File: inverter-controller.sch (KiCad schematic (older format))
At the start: 0 parts

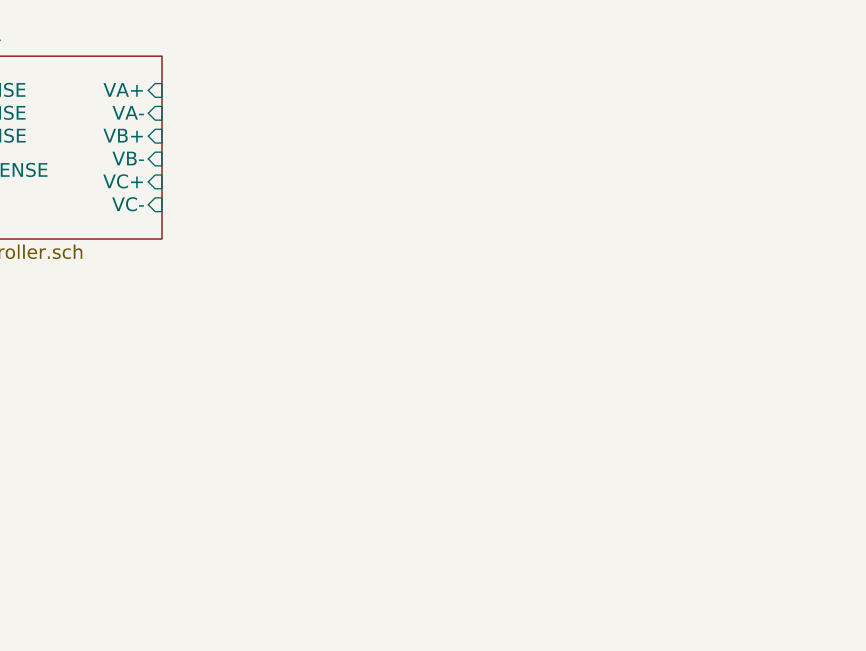
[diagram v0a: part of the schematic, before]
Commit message: Adding IGBT connectors.
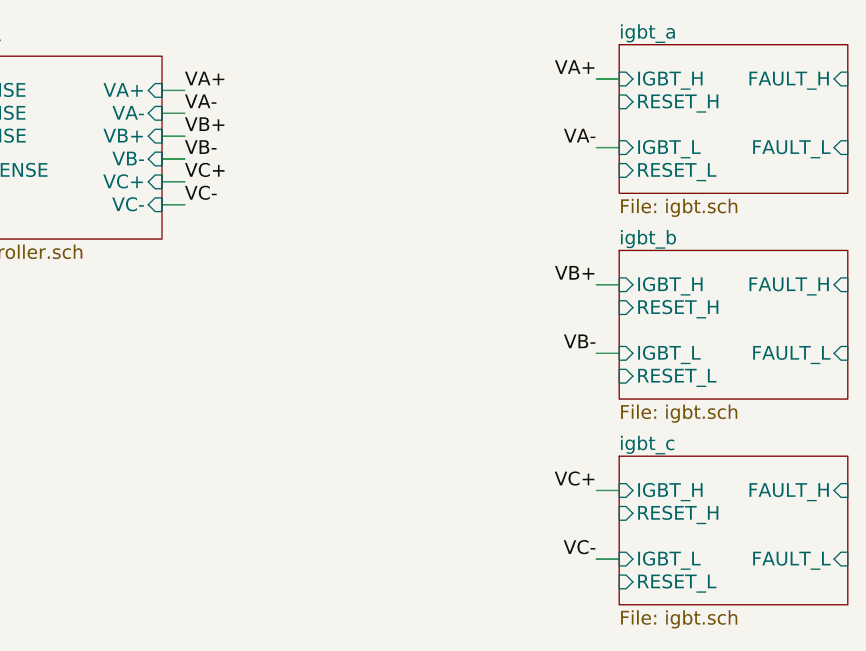
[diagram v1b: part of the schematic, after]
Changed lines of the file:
@@
 LIBS:valves
 LIBS:inverter-controller
+LIBS:inverter-controller-cache
 EELAYER 25 0
 EELAYER END
 $Descr A4 11693 8268
 encoding utf-8
-Sheet 1 3
+Sheet 1 6
 Title ""
 Date ""
@@
 Wire Wire Line
 	1400 1150 2750 1150
+$Sheet
+S 5850 600  1000 650
+U 5AED5DDF
+F0 "igbt_a" 60
+F1 "igbt.sch" 60
+F2 "IGBT_H" I L 5850 750 60
+F3 "IGBT_L" I L 5850 1050 60
+F4 "FAULT_H" I R 6850 750 60
+F5 "RESET_H" I L 5850 850 60
+F6 "FAULT_L" I R 6850 1050 60
+F7 "RESET_L" I L 5850 1150 60
+$EndSheet
+Text Label 3950 800  0    60   ~ 0
+VA+
+Text Label 3950 900  0    60   ~ 0
+VA-
+Text Label 3950 1000 0    60   ~ 0
+VB+
+Text Label 3950 1100 0    60   ~ 0
+VB-
+Text Label 3950 1200 0    60   ~ 0
+VC+
+Text Label 3950 1300 0    60   ~ 0
+VC-
+Text Label 5750 750  2    60   ~ 0
+VA+
+Text Label 5750 1050 2    60   ~ 0
+VA-
+Wire Wire Line
+	5750 750  5850 750
+Wire Wire Line
+	5750 1050 5850 1050
+Wire Wire Line
+	3950 800  3850 800
+Wire Wire Line
+	3850 900  3950 900
+Wire Wire Line
+	3850 1000 3950 1000
+Wire Wire Line
+	3850 1100 3950 1100
+Wire Wire Line
+	3850 1200 3950 1200
+Wire Wire Line
+	3850 1300 3950 1300
+$Sheet
+S 5850 1500 1000 650
+U 5AEDA321
+F0 "igbt_b" 60
+F1 "igbt.sch" 60
+F2 "IGBT_H" I L 5850 1650 60
+F3 "IGBT_L" I L 5850 1950 60
+F4 "FAULT_H" I R 6850 1650 60
+F5 "RESET_H" I L 5850 1750 60
+F6 "FAULT_L" I R 6850 1950 60
+F7 "RESET_L" I L 5850 2050 60
+$EndSheet
+Text Label 5750 1650 2    60   ~ 0
+VB+
+Text Label 5750 1950 2    60   ~ 0
+VB-
+Wire Wire Line
+	5750 1650 5850 1650
+Wire Wire Line
+	5750 1950 5850 1950
+$Sheet
+S 5850 2400 1000 650
+U 5AEDAF6D
+F0 "igbt_c" 60
+F1 "igbt.sch" 60
+F2 "IGBT_H" I L 5850 2550 60
+F3 "IGBT_L" I L 5850 2850 60
+F4 "FAULT_H" I R 6850 2550 60
+F5 "RESET_H" I L 5850 2650 60
+F6 "FAULT_L" I R 6850 2850 60
+F7 "RESET_L" I L 5850 2950 60
+$EndSheet
+Text Label 5750 2550 2    60   ~ 0
+VC+
+Text Label 5750 2850 2    60   ~ 0
+VC-
+Wire Wire Line
+	5750 2550 5850 2550
+Wire Wire Line
+	5750 2850 5850 2850
 $EndSCHEMATC

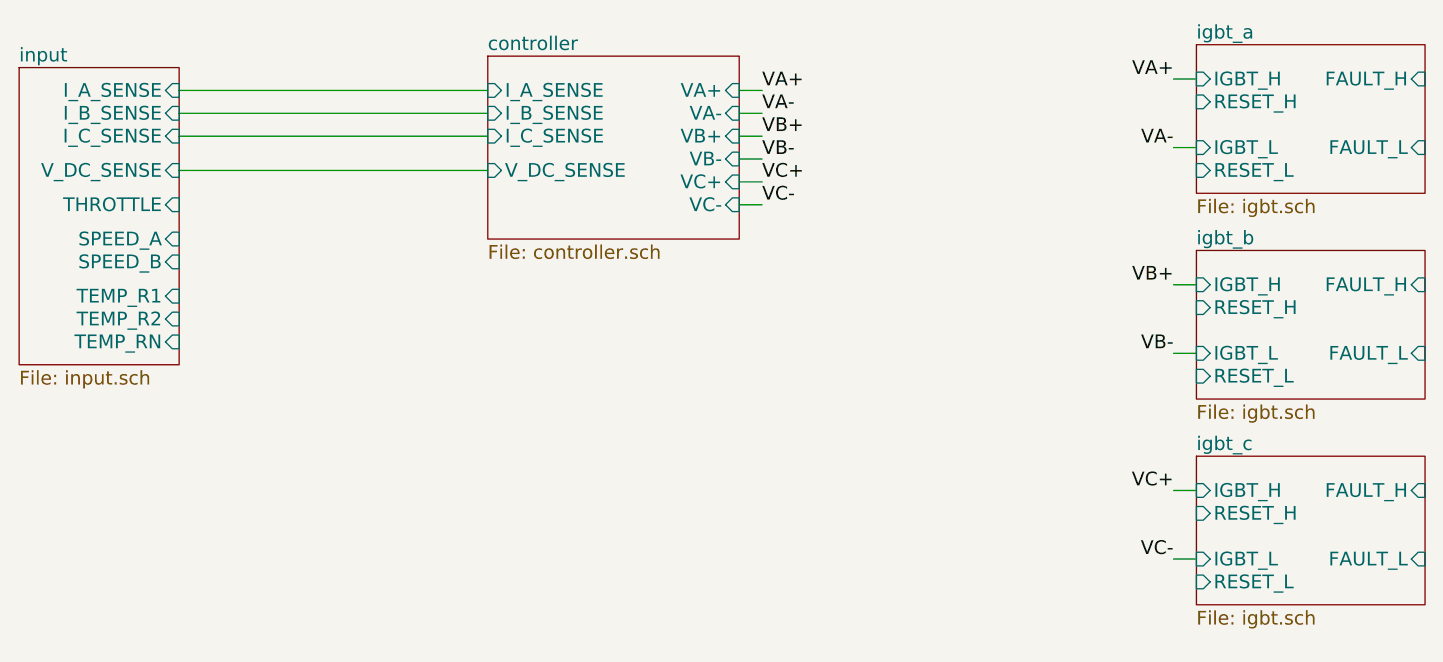
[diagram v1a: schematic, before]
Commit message: Break up input into separate schematics.
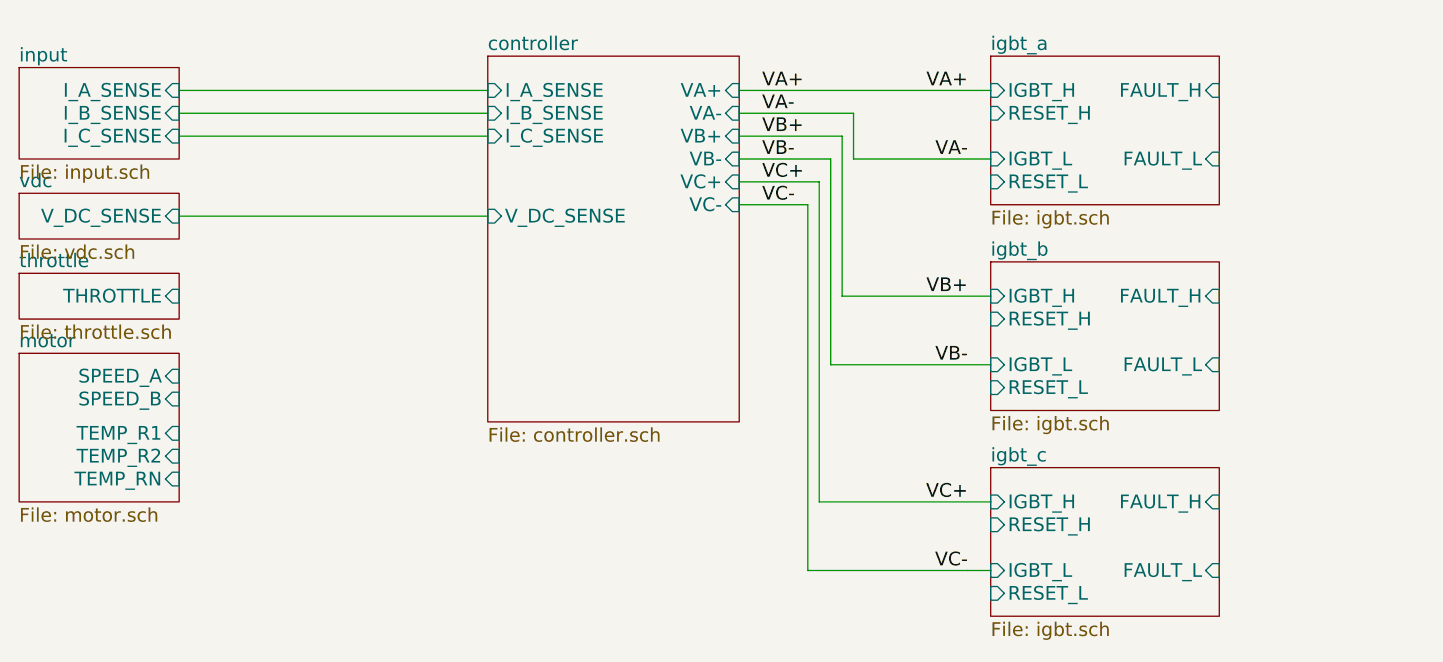
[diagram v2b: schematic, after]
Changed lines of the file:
@@
 $Descr A4 11693 8268
 encoding utf-8
-Sheet 1 6
+Sheet 1 9
 Title ""
 Date ""
@@
 $EndDescr
 $Sheet
-S 2750 650  1100 800
+S 2750 650  1100 1600
 U 5AEC1F05
 F0 "controller" 60
@@
 F9 "I_B_SENSE" I L 2750 900 60
 F10 "I_C_SENSE" I L 2750 1000 60
-F11 "V_DC_SENSE" I L 2750 1150 60
+F11 "V_DC_SENSE" I L 2750 1350 60
 $EndSheet
 $Sheet
-S 700  700  700  1300
-U 5AEC7636
-F0 "input" 60
-F1 "input.sch" 60
-F2 "I_A_SENSE" I R 1400 800 60
-F3 "I_B_SENSE" I R 1400 900 60
-F4 "I_C_SENSE" I R 1400 1000 60
-F5 "V_DC_SENSE" I R 1400 1150 60
-F6 "THROTTLE" I R 1400 1300 60
-F7 "SPEED_A" I R 1400 1450 60
-F8 "SPEED_B" I R 1400 1550 60
-F9 "TEMP_R1" I R 1400 1700 60
-F10 "TEMP_R2" I R 1400 1800 60
-F11 "TEMP_RN" I R 1400 1900 60
-$EndSheet
-Wire Wire Line
-	1400 800  2750 800
-Wire Wire Line
-	1400 900  2750 900
-Wire Wire Line
-	1400 1000 2750 1000
-Wire Wire Line
-	1400 1150 2750 1150
-$Sheet
-S 5850 600  1000 650
+S 4950 650  1000 650
 U 5AED5DDF
 F0 "igbt_a" 60
 F1 "igbt.sch" 60
-F2 "IGBT_H" I L 5850 750 60
-F3 "IGBT_L" I L 5850 1050 60
-F4 "FAULT_H" I R 6850 750 60
-F5 "RESET_H" I L 5850 850 60
-F6 "FAULT_L" I R 6850 1050 60
-F7 "RESET_L" I L 5850 1150 60
+F2 "IGBT_H" I L 4950 800 60
+F3 "IGBT_L" I L 4950 1100 60
+F4 "FAULT_H" I R 5950 800 60
+F5 "RESET_H" I L 4950 900 60
+F6 "FAULT_L" I R 5950 1100 60
+F7 "RESET_L" I L 4950 1200 60
 $EndSheet
 Text Label 3950 800  0    60   ~ 0
@@
 Text Label 3950 1300 0    60   ~ 0
 VC-
-Text Label 5750 750  2    60   ~ 0
-VA+
-Text Label 5750 1050 2    60   ~ 0
-VA-
-Wire Wire Line
-	5750 750  5850 750
-Wire Wire Line
-	5750 1050 5850 1050
-Wire Wire Line
-	3950 800  3850 800
-Wire Wire Line
-	3850 900  3950 900
-Wire Wire Line
-	3850 1000 3950 1000
-Wire Wire Line
-	3850 1100 3950 1100
-Wire Wire Line
-	3850 1200 3950 1200
-Wire Wire Line
-	3850 1300 3950 1300
 $Sheet
-S 5850 1500 1000 650
+S 4950 1550 1000 650
 U 5AEDA321
 F0 "igbt_b" 60
 F1 "igbt.sch" 60
-F2 "IGBT_H" I L 5850 1650 60
-F3 "IGBT_L" I L 5850 1950 60
-F4 "FAULT_H" I R 6850 1650 60
-F5 "RESET_H" I L 5850 1750 60
-F6 "FAULT_L" I R 6850 1950 60
-F7 "RESET_L" I L 5850 2050 60
+F2 "IGBT_H" I L 4950 1700 60
+F3 "IGBT_L" I L 4950 2000 60
+F4 "FAULT_H" I R 5950 1700 60
+F5 "RESET_H" I L 4950 1800 60
+F6 "FAULT_L" I R 5950 2000 60
+F7 "RESET_L" I L 4950 2100 60
 $EndSheet
-Text Label 5750 1650 2    60   ~ 0
-VB+
-Text Label 5750 1950 2    60   ~ 0
-VB-
-Wire Wire Line
-	5750 1650 5850 1650
-Wire Wire Line
-	5750 1950 5850 1950
 $Sheet
-S 5850 2400 1000 650
+S 4950 2450 1000 650
 U 5AEDAF6D
 F0 "igbt_c" 60
 F1 "igbt.sch" 60
-F2 "IGBT_H" I L 5850 2550 60
-F3 "IGBT_L" I L 5850 2850 60
-F4 "FAULT_H" I R 6850 2550 60
-F5 "RESET_H" I L 5850 2650 60
-F6 "FAULT_L" I R 6850 2850 60
-F7 "RESET_L" I L 5850 2950 60
+F2 "IGBT_H" I L 4950 2600 60
+F3 "IGBT_L" I L 4950 2900 60
+F4 "FAULT_H" I R 5950 2600 60
+F5 "RESET_H" I L 4950 2700 60
+F6 "FAULT_L" I R 5950 2900 60
+F7 "RESET_L" I L 4950 3000 60
 $EndSheet
-Text Label 5750 2550 2    60   ~ 0
+$Sheet
+S 700  1950 700  650
+U 5AEDE197
+F0 "motor" 60
+F1 "motor.sch" 60
+F2 "SPEED_A" I R 1400 2050 60
+F3 "SPEED_B" I R 1400 2150 60
+F4 "TEMP_R1" I R 1400 2300 60
+F5 "TEMP_R2" I R 1400 2400 60
+F6 "TEMP_RN" I R 1400 2500 60
+$EndSheet
+$Sheet
+S 700  700  700  400
+U 5AEC7636
+F0 "input" 60
+F1 "input.sch" 60
+F2 "I_A_SENSE" I R 1400 800 60
+F3 "I_B_SENSE" I R 1400 900 60
+F4 "I_C_SENSE" I R 1400 1000 60
+$EndSheet
+$Sheet
+S 700  1600 700  200
+U 5AEE00A3
+F0 "throttle" 60
+F1 "throttle.sch" 60
+F2 "THROTTLE" I R 1400 1700 60
+$EndSheet
+$Sheet
+S 700  1250 700  200
+U 5AEE7A72
+F0 "vdc" 60
+F1 "vdc.sch" 60
+F2 "V_DC_SENSE" I R 1400 1350 60
+$EndSheet
+Wire Wire Line
+	1400 800  2750 800
+Wire Wire Line
+	1400 900  2750 900
+Wire Wire Line
+	1400 1000 2750 1000
+Wire Wire Line
+	3850 800  4950 800
+Wire Wire Line
+	4350 1100 4950 1100
+Wire Wire Line
+	3850 900  4350 900
+Wire Wire Line
+	3850 1000 4300 1000
+Wire Wire Line
+	3850 1100 4250 1100
+Wire Wire Line
+	3850 1200 4200 1200
+Wire Wire Line
+	3850 1300 4150 1300
+Wire Wire Line
+	4300 1700 4950 1700
+Wire Wire Line
+	4250 2000 4950 2000
+Wire Wire Line
+	4200 2600 4950 2600
+Wire Wire Line
+	2750 1350 1400 1350
+Wire Wire Line
+	4350 900  4350 1100
+Wire Wire Line
+	4300 1000 4300 1700
+Wire Wire Line
+	4250 1100 4250 2000
+Wire Wire Line
+	4200 1200 4200 2600
+Wire Wire Line
+	4150 2900 4150 1300
+Wire Wire Line
+	4850 2900 4950 2900
+Wire Wire Line
+	4850 2900 4150 2900
+Text Label 4850 2900 2    60   ~ 0
+VC-
+Text Label 4850 2600 2    60   ~ 0
 VC+
-Text Label 5750 2850 2    60   ~ 0
-VC-
-Wire Wire Line
-	5750 2550 5850 2550
-Wire Wire Line
-	5750 2850 5850 2850
+Text Label 4850 2000 2    60   ~ 0
+VB-
+Text Label 4850 1700 2    60   ~ 0
+VB+
+Text Label 4850 1100 2    60   ~ 0
+VA-
+Text Label 4850 800  2    60   ~ 0
+VA+
 $EndSCHEMATC

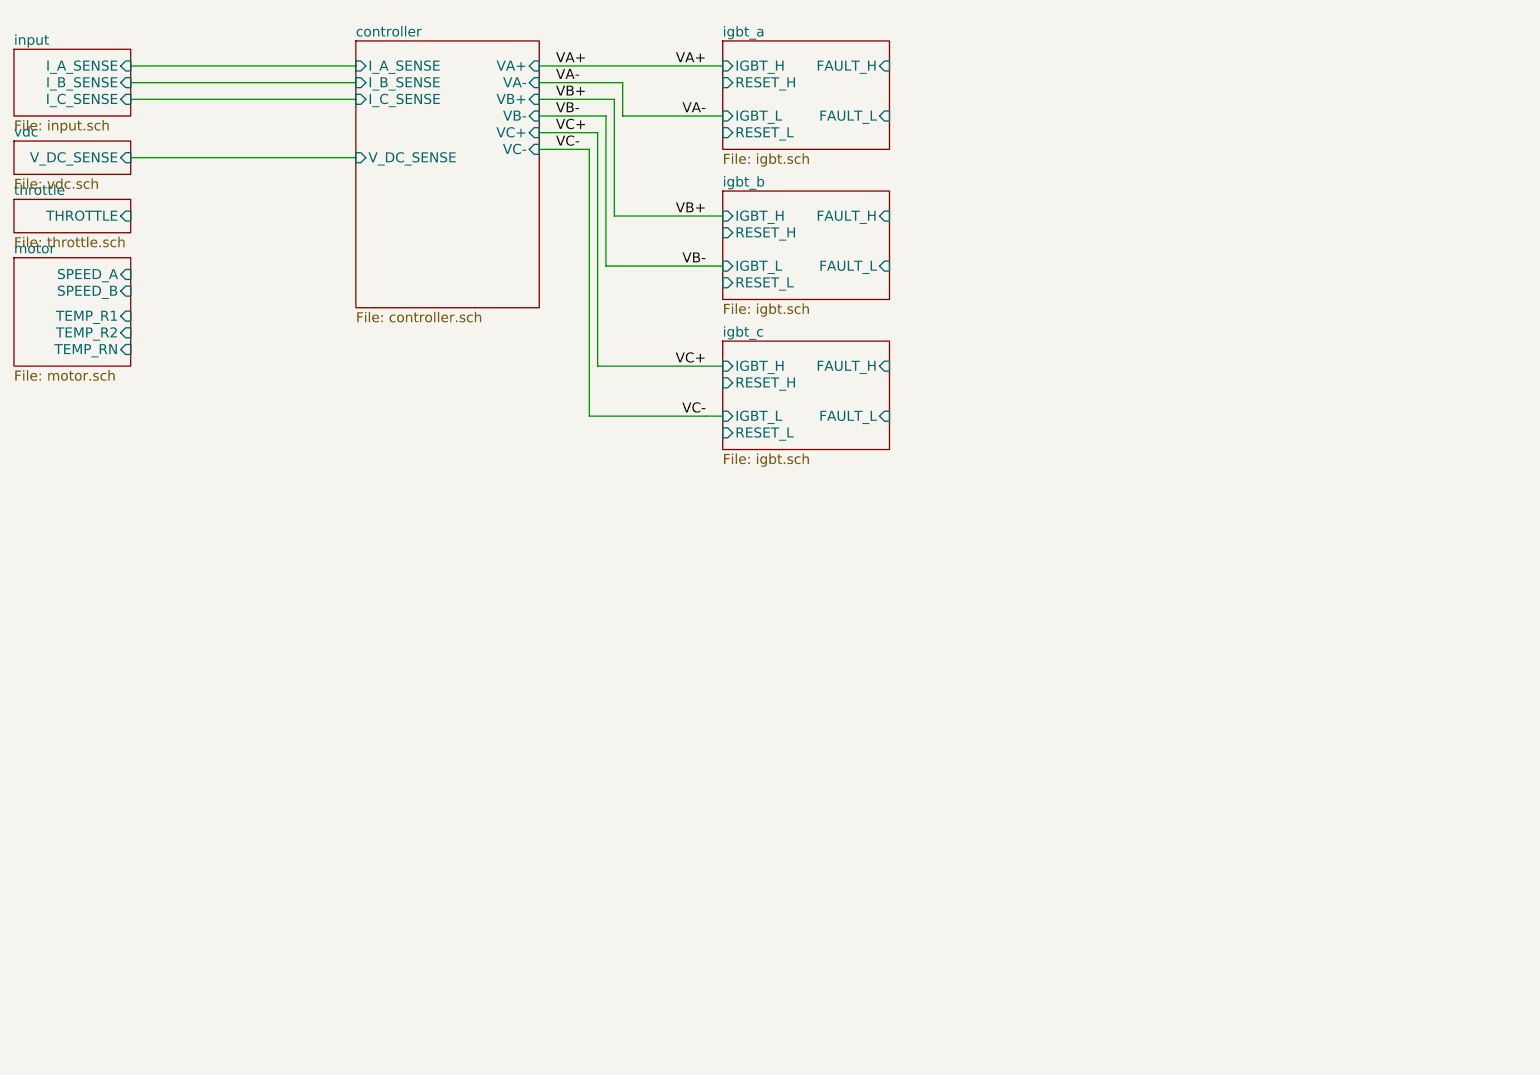
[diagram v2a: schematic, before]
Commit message: Implementing more faults and organizing.
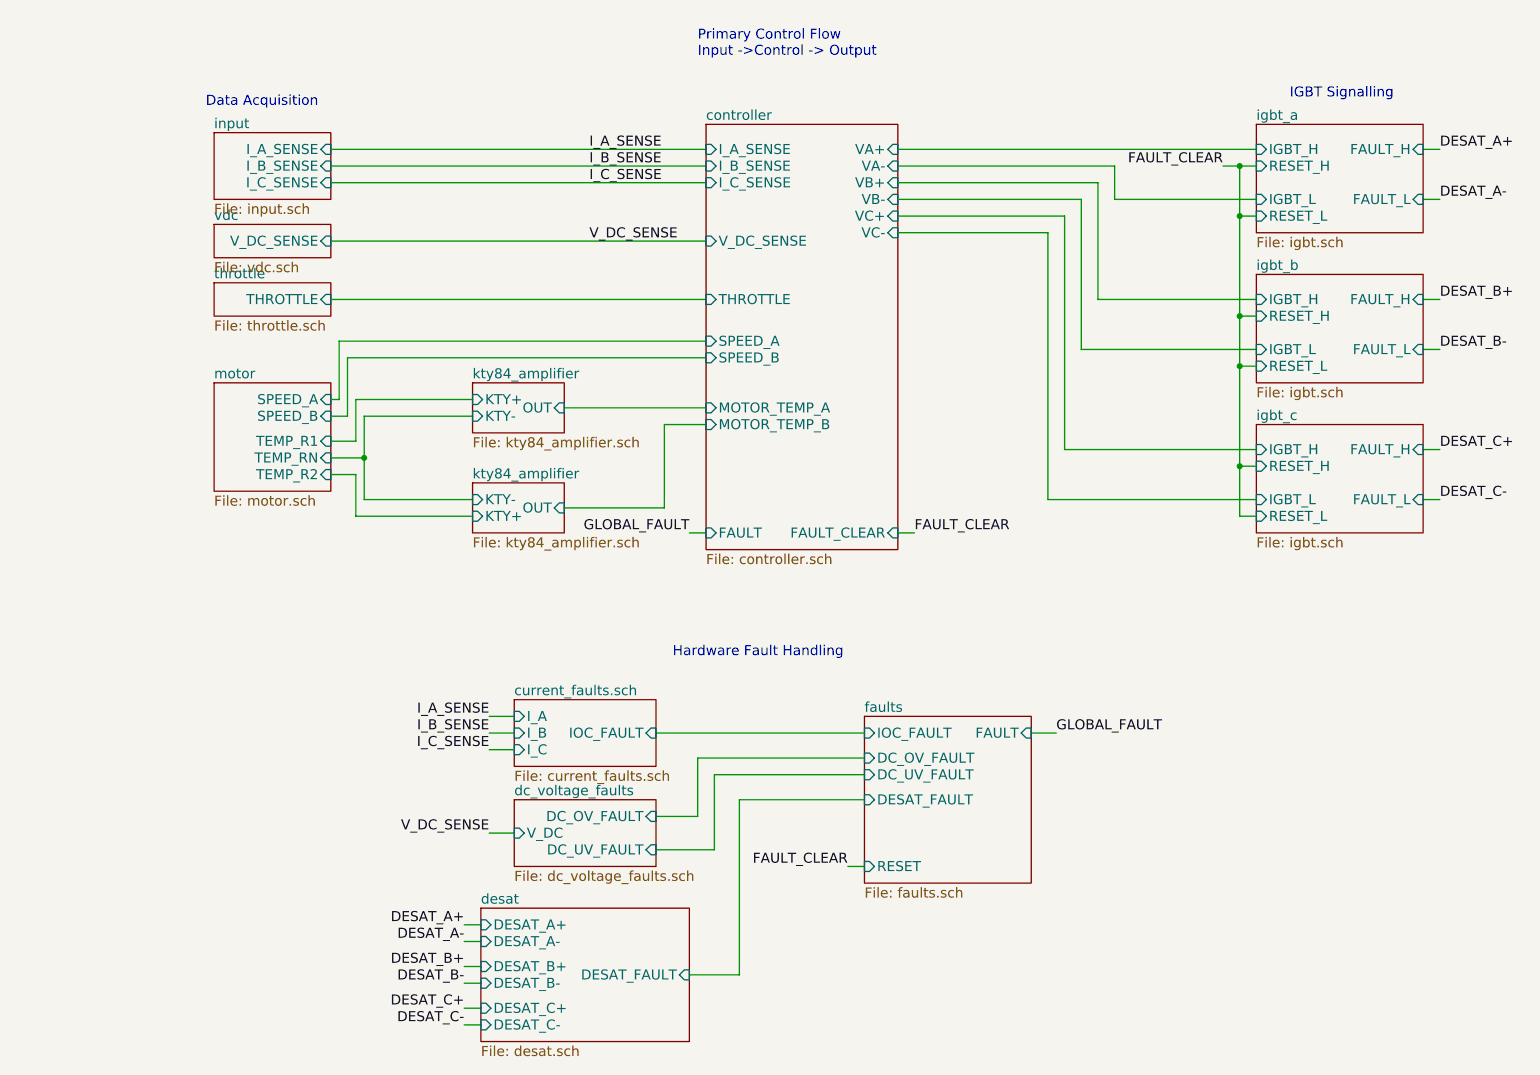
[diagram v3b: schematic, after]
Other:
- note added: "Data Acquisition"
- note added: "Hardware Fault Handling"
- note added: "IGBT Signalling"
- note added: "Primary Control Flow\nInput ->Control -> Output"
